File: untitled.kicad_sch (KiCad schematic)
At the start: 14 parts, among them J4 Pyro 2, J5 Pyro 1, Q1 FDS9926A, Q2 FDS4953

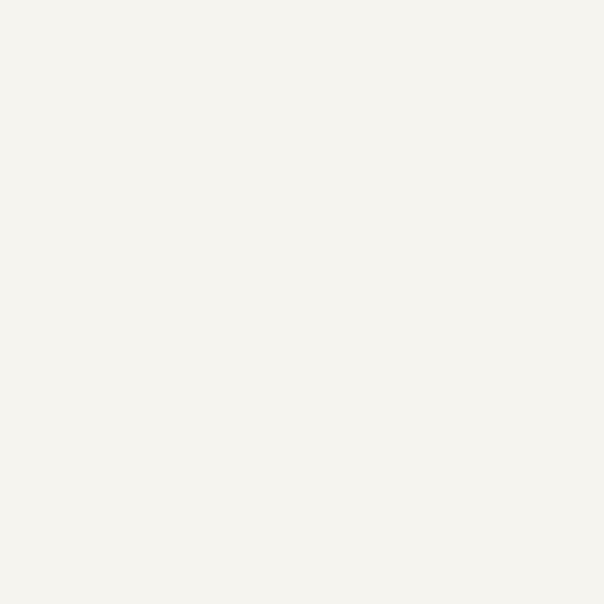
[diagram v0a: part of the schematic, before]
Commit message: 0.2
PCB edit
Added 3D models
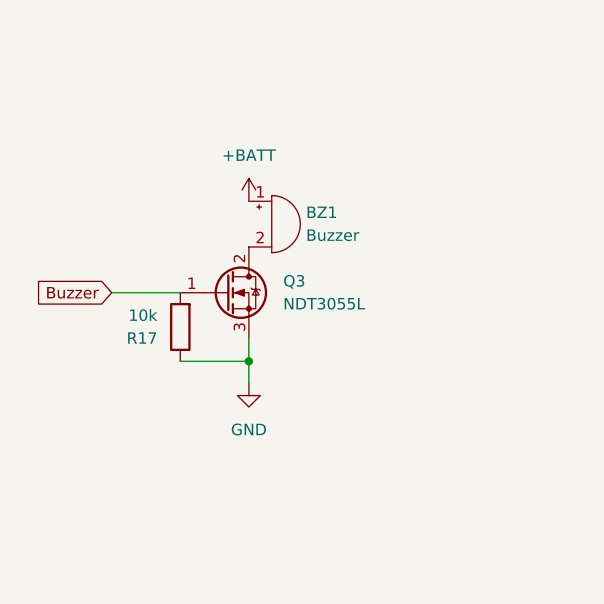
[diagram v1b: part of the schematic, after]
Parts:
- added BZ1: Buzzer, Buzzer_Beeper:Buzzer_Murata_PKMCS0909E, symbol Device:Buzzer
- added Q3: NDT3055L, Package_TO_SOT_SMD:TSOT-23_HandSoldering, symbol Transistor_FET:NDT3055L
- added R17: 10k, Resistor_SMD:R_0603_1608Metric_Pad0.98x0.95mm_HandSolder, symbol Device:R
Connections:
- net +BATT: now also BZ1.1 (-)
- net GND: now also Q3.3 (S), R17.1
- new net: BZ1.2 (+), Q3.2 (D)
- new net Buzzer: Q3.1 (G), R17.2
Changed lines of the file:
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@@
 (kicad_sch (version 20211123) (generator eeschema)
   (paper "A4")
+  (junction (at 154.94 60.96) (diameter 0) (color 0 0 0 0)
+  )
   (junction (at 224.79 109.22) (diameter 0) (color 0 0 0 0)
   )
@@
   (junction (at 242.57 101.6) (diameter 0) (color 0 0 0 0)
   )
+  (wire (pts (xy 147.32 60.96) (xy 154.94 60.96))
+    (stroke (width 0) (type default) (color 0 0 0 0))
+  )
   (wire (pts (xy 209.55 114.3) (xy 217.17 114.3))
     (stroke (width 0) (type default) (color 0 0 0 0))
@@
     (stroke (width 0) (type default) (color 0 0 0 0))
   )
+  (wire (pts (xy 154.94 58.42) (xy 154.94 60.96))
+    (stroke (width 0) (type default) (color 0 0 0 0))
+  )
   (wire (pts (xy 256.54 29.21) (xy 256.54 30.48))
     (stroke (width 0) (type default) (color 0 0 0 0))
   )
+  (wire (pts (xy 139.7 53.34) (xy 147.32 53.34))
+    (stroke (width 0) (type default) (color 0 0 0 0))
+  )
   (wire (pts (xy 215.9 67.31) (xy 223.52 67.31))
     (stroke (width 0) (type default) (color 0 0 0 0))
   )
   (wire (pts (xy 224.79 119.38) (xy 224.79 121.92))
+    (stroke (width 0) (type default) (color 0 0 0 0))
+  )
+  (wire (pts (xy 154.94 60.96) (xy 154.94 63.5))
     (stroke (width 0) (type default) (color 0 0 0 0))
   )
@@
     )
   )
+  (global_label "Buzzer" (shape input) (at 139.7 53.34 180) (fields_autoplaced)
+    (effects (font (size 1.27 1.27)) (justify right))
+    (property "Intersheet References" "${INTERSHEET_REFS}" (id 0) (at 130.9369 53.2606 0)
+      (effects (font (size 1.27 1.27)) (justify right) hide)
+    )
+  )
   (symbol (lib_id "power:+BATT") (at 256.54 87.63 0) (unit 1)
     (in_bom yes) (on_board yes) (fields_autoplaced)
@@
     (pin "2")
   )
+  (symbol (lib_id "power:+BATT") (at 154.94 43.18 0) (unit 1)
+    (in_bom yes) (on_board yes) (fields_autoplaced)
+    (property "Reference" "#PWR0158" (id 0) (at 154.94 46.99 0)
+      (effects (font (size 1.27 1.27)) hide)
+    )
+    (property "Value" "+BATT" (id 1) (at 154.94 38.1 0))
+    (property "Footprint" "" (id 2) (at 154.94 43.18 0)
+      (effects (font (size 1.27 1.27)) hide)
+    )
+    (property "Datasheet" "" (id 3) (at 154.94 43.18 0)
+      (effects (font (size 1.27 1.27)) hide)
+    )
+    (pin "1")
+  )
+  (symbol (lib_id "Transistor_FET:NDT3055L") (at 152.4 53.34 0) (unit 1)
+    (in_bom yes) (on_board yes) (fields_autoplaced)
+    (property "Reference" "Q3" (id 0) (at 158.75 52.0699 0)
+      (effects (font (size 1.27 1.27)) (justify left))
+    )
+    (property "Value" "NDT3055L" (id 1) (at 158.75 54.6099 0)
+      (effects (font (size 1.27 1.27)) (justify left))
+    )
+    (property "Footprint" "Package_TO_SOT_SMD:TSOT-23_HandSoldering" (id 2) (at 157.48 57.15 0)
+      (effects (font (size 1.27 1.27)) (justify left) hide)
+    )
+    (property "Datasheet" "https://www.onsemi.com/pdf/datasheet/ndt3055l-d.pdf" (id 3) (at 157.48 48.26 0)
+      (effects (font (size 1.27 1.27)) (justify left) hide)
+    )
+    (pin "1")
+    (pin "2")
+    (pin "3")
+  )
   (symbol (lib_id "power:GND") (at 241.3 59.69 0) (unit 1)
     (in_bom yes) (on_board yes) (fields_autoplaced)
@@
     (pin "7")
     (pin "8")
+  )
+  (symbol (lib_id "Device:Buzzer") (at 157.48 45.72 0) (unit 1)
+    (in_bom yes) (on_board yes) (fields_autoplaced)
+    (property "Reference" "BZ1" (id 0) (at 161.29 44.4499 0)
+      (effects (font (size 1.27 1.27)) (justify left))
+    )
+    (property "Value" "Buzzer" (id 1) (at 161.29 46.9899 0)
+      (effects (font (size 1.27 1.27)) (justify left))
+    )
+    (property "Footprint" "Buzzer_Beeper:Buzzer_Murata_PKMCS0909E" (id 2) (at 156.845 43.18 90)
+      (effects (font (size 1.27 1.27)) hide)
+    )
+    (property "Datasheet" "~" (id 3) (at 156.845 43.18 90)
+      (effects (font (size 1.27 1.27)) hide)
+    )
+    (pin "1")
+    (pin "2")
   )
   (symbol (lib_id "FDS4953:FDS4953") (at 240.03 109.22 0) (unit 1)
@@
     (pin "2")
   )
+  (symbol (lib_id "Device:R") (at 147.32 57.15 180) (unit 1)
+    (in_bom yes) (on_board yes) (fields_autoplaced)
+    (property "Reference" "R17" (id 0) (at 144.78 58.4201 0)
+      (effects (font (size 1.27 1.27)) (justify left))
+    )
+    (property "Value" "10k" (id 1) (at 144.78 55.8801 0)
+      (effects (font (size 1.27 1.27)) (justify left))
+    )
+    (property "Footprint" "Resistor_SMD:R_0603_1608Metric_Pad0.98x0.95mm_HandSolder" (id 2) (at 149.098 57.15 90)
+      (effects (font (size 1.27 1.27)) hide)
+    )
+    (property "Datasheet" "~" (id 3) (at 147.32 57.15 0)
+      (effects (font (size 1.27 1.27)) hide)
+    )
+    (pin "1")
+    (pin "2")
+  )
   (symbol (lib_id "Device:LED") (at 256.54 63.5 90) (unit 1)
     (in_bom yes) (on_board yes) (fields_autoplaced)
@@
     (pin "2")
   )
+  (symbol (lib_id "power:GND") (at 154.94 63.5 0) (unit 1)
+    (in_bom yes) (on_board yes) (fields_autoplaced)
+    (property "Reference" "#PWR0157" (id 0) (at 154.94 69.85 0)
+      (effects (font (size 1.27 1.27)) hide)
+    )
+    (property "Value" "GND" (id 1) (at 154.94 68.58 0))
+    (property "Footprint" "" (id 2) (at 154.94 63.5 0)
+      (effects (font (size 1.27 1.27)) hide)
+    )
+    (property "Datasheet" "" (id 3) (at 154.94 63.5 0)
+      (effects (font (size 1.27 1.27)) hide)
+    )
+    (pin "1")
+  )
   (symbol (lib_id "power:GND") (at 256.54 69.85 0) (unit 1)

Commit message: Rework for prototype 2
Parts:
- added R18: 1k, Resistor_SMD:R_0603_1608Metric_Pad0.98x0.95mm_HandSolder, symbol Device:R
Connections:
- net +BATT: now also R18.2
- net at BZ1.2 (+), Q3.2 (D): now also R18.1
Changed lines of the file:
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@@
   (junction (at 256.54 101.6) (diameter 0) (color 0 0 0 0)
   )
+  (junction (at 147.32 53.34) (diameter 0) (color 0 0 0 0)
+  )
   (junction (at 217.17 114.3) (diameter 0) (color 0 0 0 0)
   )
   (junction (at 215.9 59.69) (diameter 0) (color 0 0 0 0)
   )
+  (junction (at 154.94 48.26) (diameter 0) (color 0 0 0 0)
+  )
   (junction (at 241.3 43.18) (diameter 0) (color 0 0 0 0)
   )
+  (junction (at 154.94 43.18) (diameter 0) (color 0 0 0 0)
+  )
   (junction (at 223.52 53.34) (diameter 0) (color 0 0 0 0)
   )
@@
     (stroke (width 0) (type default) (color 0 0 0 0))
   )
+  (wire (pts (xy 149.86 43.18) (xy 149.86 41.91))
+    (stroke (width 0) (type default) (color 0 0 0 0))
+  )
   (wire (pts (xy 242.57 101.6) (xy 256.54 101.6))
     (stroke (width 0) (type default) (color 0 0 0 0))
@@
     (stroke (width 0) (type default) (color 0 0 0 0))
   )
+  (wire (pts (xy 149.86 48.26) (xy 154.94 48.26))
+    (stroke (width 0) (type default) (color 0 0 0 0))
+  )
+  (wire (pts (xy 149.86 41.91) (xy 147.32 41.91))
+    (stroke (width 0) (type default) (color 0 0 0 0))
+  )
+  (wire (pts (xy 149.86 49.53) (xy 147.32 49.53))
+    (stroke (width 0) (type default) (color 0 0 0 0))
+  )
   (wire (pts (xy 208.28 59.69) (xy 215.9 59.69))
     (stroke (width 0) (type default) (color 0 0 0 0))
   )
+  (wire (pts (xy 149.86 43.18) (xy 154.94 43.18))
+    (stroke (width 0) (type default) (color 0 0 0 0))
+  )
   (wire (pts (xy 256.54 110.49) (xy 256.54 101.6))
     (stroke (width 0) (type default) (color 0 0 0 0))
@@
   )
   (wire (pts (xy 236.22 53.34) (xy 236.22 50.8))
+    (stroke (width 0) (type default) (color 0 0 0 0))
+  )
+  (wire (pts (xy 149.86 48.26) (xy 149.86 49.53))
     (stroke (width 0) (type default) (color 0 0 0 0))
   )
@@
     (pin "6")
   )
+  (symbol (lib_id "Device:R") (at 147.32 45.72 0) (mirror x) (unit 1)
+    (in_bom yes) (on_board yes) (fields_autoplaced)
+    (property "Reference" "R18" (id 0) (at 144.78 44.4499 0)
+      (effects (font (size 1.27 1.27)) (justify right))
+    )
+    (property "Value" "1k" (id 1) (at 144.78 46.9899 0)
+      (effects (font (size 1.27 1.27)) (justify right))
+    )
+    (property "Footprint" "Resistor_SMD:R_0603_1608Metric_Pad0.98x0.95mm_HandSolder" (id 2) (at 145.542 45.72 90)
+      (effects (font (size 1.27 1.27)) hide)
+    )
+    (property "Datasheet" "~" (id 3) (at 147.32 45.72 0)
+      (effects (font (size 1.27 1.27)) hide)
+    )
+    (pin "1")
+    (pin "2")
+  )
   (symbol (lib_id "power:GND") (at 223.52 67.31 0) (unit 1)

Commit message: V3
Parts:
- J4: footprint TerminalBlock_4Ucon:TerminalBlock_4Ucon_1x02_P3.50mm_Vertical -> TerminalBlock_Phoenix:TerminalBlock_Phoenix_MPT-0,5-2-2.54_1x02_P2.54mm_Horizontal
- J5: value Pyro 1 -> Pyro 2; footprint TerminalBlock_4Ucon:TerminalBlock_4Ucon_1x02_P3.50mm_Vertical -> TerminalBlock_Phoenix:TerminalBlock_Phoenix_MPT-0,5-2-2.54_1x02_P2.54mm_Horizontal
- Q3: footprint Package_TO_SOT_SMD:TSOT-23_HandSoldering -> Package_TO_SOT_SMD:TSOT-23
- R10, R11, R12, R13, R14, R15, R17, R18: footprint Resistor_SMD:R_0603_1608Metric_Pad0.98x0.95mm_HandSolder -> Resistor_SMD:R_0402_1005Metric_Pad0.72x0.64mm_HandSolder
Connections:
- net +BATT: now also Q2.1, Q2.3, R12.2, R13.2, R14.1, R15.1; no longer F1.1, F2.1
- net GND: now also J4.2 (Pin_2), J5.2 (Pin_2); no longer D5.1 (K), D6.1 (K), Q2.5, Q2.6, Q2.7, Q2.8
- net P1_EN: now also Q1.4 (G2); no longer Q1.2 (G1)
- net P2_EN: now also Q1.2 (G1); no longer Q1.4 (G2)
- net at F2.2, J5.1 (Pin_1): now also D6.1 (K)
- net at Q2.2, R12.1: now also Q1.7 (D1), Q1.8 (D1); no longer Q1.5 (D2), Q1.6 (D2)
- net at Q2.4, R13.1: now also Q1.5 (D2), Q1.6 (D2); no longer Q1.7 (D1), Q1.8 (D1)
- net at F1.2, J4.1 (Pin_1): now also D5.1 (K)
- new net: F2.1, Q2.5, Q2.6
- new net: F1.1, Q2.7, Q2.8
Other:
- moved on the sheet: D5, D6, F1, F2, Q1A, Q1B, R14, R15

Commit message: Rev 27052023
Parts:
- added D7: APA102-2020, LED_SMD:LED-APA102-2020, symbol LED:APA102-2020
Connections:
- net GND: now also D7.6 (GND)
- new net +3V3: D7.1 (VDD)
- new net CI: D7.5 (CKI)
- new net DI: D7.4 (SDI)
- no-connect marks 0 -> 2
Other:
- note added: "Buzzer"
- note added: "Pyro channels"
- note added: "Status LED"
- moved on the sheet: BZ1, D5, D6, F1, F2, Q1A, Q1B, Q2A, Q2B, Q3, R10, R11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
